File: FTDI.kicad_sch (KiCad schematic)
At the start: 24 parts, among them J301 Conn_01x02_Male, J302 Conn_01x03_Male, SW301 SW_SPDT, U301 SN74LVC257AD, U302 FT232HL, U303 93LC56BT-I/OT, Y301 12MHz

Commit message: Complete Draft 1 of PCB Design
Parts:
- removed J301: Conn_01x02_Male, Connector_PinHeader_2.54mm:PinHeader_1x02_P2.54mm_Vertical, symbol Connector:Conn_01x02_Male
- removed R305: 10K, Resistor_SMD:R_0402_1005Metric, symbol Device:R
- removed SW301: SW_SPDT, Button_Switch_SMD:SW_SPDT_PCM12, symbol Switch:SW_SPDT
- added J301: Conn_01x04_Male, Connector_PinHeader_2.54mm:PinHeader_1x04_P2.54mm_Horizontal, symbol Connector:Conn_01x04_Male
- added J302: Conn_01x03_Male, Connector_PinHeader_2.54mm:PinHeader_1x03_P2.54mm_Horizontal, symbol Connector:Conn_01x03_Male
- renumbered J302 to J303, R306 to R305
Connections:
- net +3V3: now also J302.1 (Pin_1)
- net CONN.SCK: now also J301.2 (Pin_2), J301.4 (Pin_4)
- net CONN.SDA: now also J301.1 (Pin_1), J301.3 (Pin_3)
- net GND: now also J302.3 (Pin_3)
- net MUX.SEL: now also J302.2 (Pin_2)
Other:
- note removed: "Default = FTDI"

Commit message: Draft 1 complete
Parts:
- removed U301: SN74LVC257AD, Package_SO:SOIC-16W_5.3x10.2mm_P1.27mm, symbol 74xx:74LS157
- C301, C302, C303, C304, C305: LCSC (none) -> C1525; LCSC Part Number (none) -> C1525
- C306, C307: LCSC (none) -> C76991; LCSC Part Number (none) -> C76991
- C308, C309: LCSC (none) -> C1557; LCSC Part Number (none) -> C1557
- FB301, FB302: LCSC (none) -> C1002; LCSC Part Number (none) -> C1002
- J301: LCSC (none) -> C91552; LCSC Part Number (none) -> C91552
- J302: footprint Connector_PinHeader_2.54mm:PinHeader_1x03_P2.54mm_Horizontal -> Connector_PinHeader_2.54mm:PinHeader_1x03_P2.54mm_Vertical; LCSC (none) -> C49257; LCSC Part Number (none) -> C49257
- J303: LCSC (none) -> C49257; LCSC Part Number (none) -> C49257
- R301, R302: LCSC (none) -> C140214; LCSC Part Number (none) -> C140214
- R303, R304: LCSC (none) -> C25752; LCSC Part Number (none) -> C25752
- R305: LCSC (none) -> C25879; LCSC Part Number (none) -> C25879
- U301: renamed from U302; value FT232HL -> FT232HQ-REEL; footprint Package_QFP:LQFP-48_7x7mm_P0.5mm -> Package_DFN_QFN:QFN-48-1EP_8x8mm_P0.5mm_EP6.2x6.2mm; LCSC (none) -> C82158; LCSC Part Number (none) -> C82158
- U302: renamed from U303; LCSC (none) -> C190271; LCSC Part Number (none) -> C190271
- Y301: LCSC (none) -> C14871; LCSC Part Number (none) -> C14871
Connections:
- net +3V3: no longer J302.1 (Pin_1), J303.1 (Pin_1)
- net CONN.SCK: now also J303.1 (Pin_1)
- net CONN.SDA: now also J302.1 (Pin_1)
- net FTDI.SCK: now also J303.3 (Pin_3)
- net FTDI.SDA: now also J302.3 (Pin_3)
- net GND: now also U301.49 (GND); no longer J302.3 (Pin_3), J303.3 (Pin_3)
- net IO.SCK: now also J303.2 (Pin_2)
- net IO.SDA: now also J302.2 (Pin_2)
- removed net MUX.SEL: J302.2 (Pin_2), J303.2 (Pin_2)
- no-connect marks 22 -> 16
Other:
- note added: "Jumper Headers for selecting FTDI or Header"
- note added: "Use jumpers to select between modes: Select CONN: CONN.SDA=IO.SDA & CONN.SCK=IO.SCK Select FTDI: FTDI.SDA=IO.SDA & FTDI.SCK=IO.SCK"
- note removed: "MUX for selecting FTDI or Header (Default=FTDI)"
- note removed: "Propagation Delay = 4.6ns"
- note removed: "SEL = L, Output = A = FTDI SEL = H, Output = B = CONN"
- moved on the sheet: J301

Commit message: Complete Design
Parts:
- J302, J303: LCSC C49257 -> (none); LCSC Part Number C49257 -> (none)
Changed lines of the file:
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@@
       (effects (font (size 1.27 1.27)) hide)
     )
-    (property "LCSC" "C49257" (id 4) (at 282.575 36.195 0)
-      (effects (font (size 1.27 1.27)) hide)
-    )
-    (property "LCSC Part Number" "C49257" (id 5) (at 282.575 36.195 0)
+    (property "LCSC" "" (id 4) (at 282.575 36.195 0)
+      (effects (font (size 1.27 1.27)) hide)
+    )
+    (property "LCSC Part Number" "" (id 5) (at 282.575 36.195 0)
       (effects (font (size 1.27 1.27)) hide)
     )
@@
       (effects (font (size 1.27 1.27)) hide)
     )
-    (property "LCSC" "C49257" (id 4) (at 285.115 36.195 0)
-      (effects (font (size 1.27 1.27)) hide)
-    )
-    (property "LCSC Part Number" "C49257" (id 5) (at 285.115 36.195 0)
-      (effects (font (size 1.27 1.27)) hide)
-    )
+    (property "LCSC" "" (id 4) (at 285.115 36.195 0)
+      (effects (font (size 1.27 1.27)) hide)
+    )
+    (property "LCSC Part Number" "" (id 5) (at 285.115 36.195 0)
+      (effects (font (size 1.27 1.27)) hide)
+    )

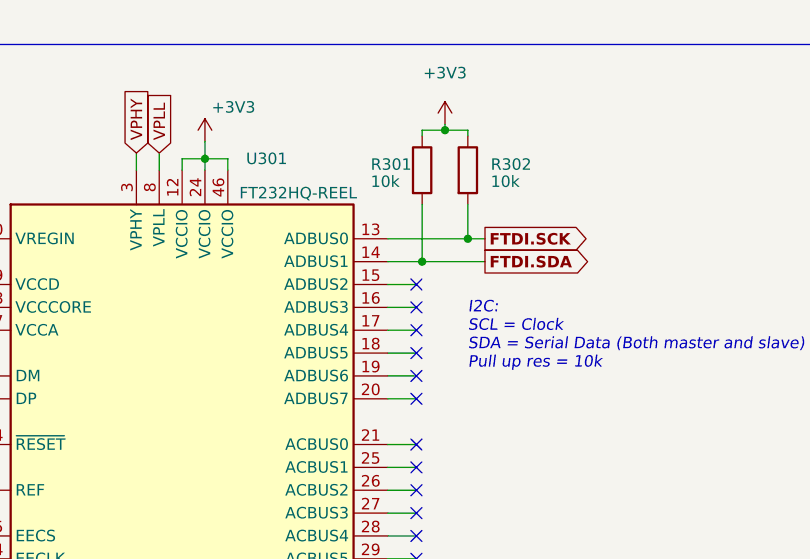
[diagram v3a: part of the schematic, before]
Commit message: Fix FTDI 1 Channel SDA issue
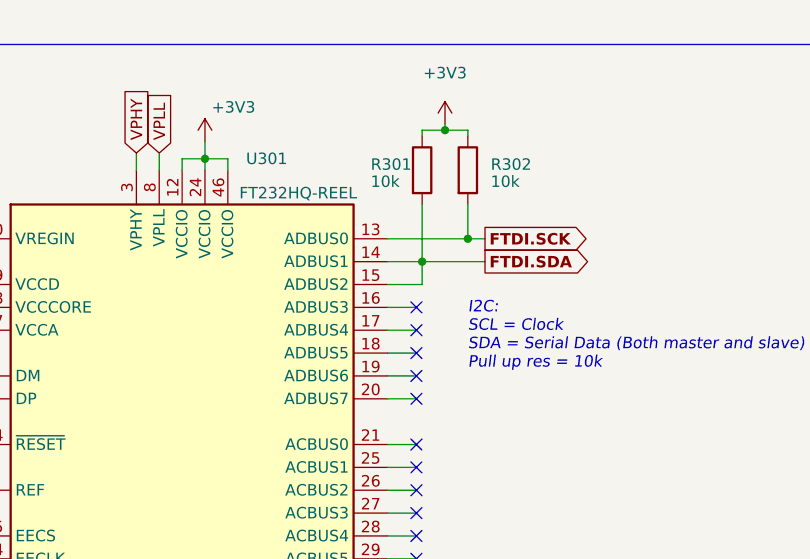
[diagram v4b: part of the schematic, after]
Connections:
- net FTDI.SDA: now also U301.15 (ADBUS2)
- no-connect marks 16 -> 15
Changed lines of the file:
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@@
   (no_connect (at 104.14 63.5))
   (no_connect (at 104.14 53.34))
-  (no_connect (at 104.14 50.8))
   (wire (pts (xy 224.155 68.58) (xy 229.235 68.58))
     (stroke (width 0) (type default) (color 0 0 0 0))
@@
     (stroke (width 0) (type default) (color 0 0 0 0))
   )
+  (wire (pts (xy 104.775 50.8) (xy 104.775 48.26))
+    (stroke (width 0) (type default) (color 0 0 0 0))
+  )
   (wire (pts (xy 104.775 48.26) (xy 111.76 48.26))
     (stroke (width 0) (type default) (color 0 0 0 0))
@@
     (stroke (width 0) (type default) (color 0 0 0 0))
   )
-  (wire (pts (xy 100.965 50.8) (xy 104.14 50.8))
-    (stroke (width 0) (type default) (color 0 0 0 0))
-  )
+  (wire (pts (xy 100.965 50.8) (xy 104.775 50.8))
+    (stroke (width 0) (type default) (color 0 0 0 0))
+  )

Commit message: Complete V1.3
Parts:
- J302, J303: LCSC (none) -> C3012205; LCSC Part Number (none) -> C3012205
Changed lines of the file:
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@@
       (effects (font (size 1.27 1.27)) hide)
     )
-    (property "LCSC" "" (id 4) (at 282.575 36.195 0)
-      (effects (font (size 1.27 1.27)) hide)
-    )
-    (property "LCSC Part Number" "" (id 5) (at 282.575 36.195 0)
+    (property "LCSC" "C3012205" (id 4) (at 282.575 36.195 0)
+      (effects (font (size 1.27 1.27)) hide)
+    )
+    (property "LCSC Part Number" "C3012205" (id 5) (at 282.575 36.195 0)
       (effects (font (size 1.27 1.27)) hide)
     )
@@
       (effects (font (size 1.27 1.27)) hide)
     )
-    (property "LCSC" "" (id 4) (at 285.115 36.195 0)
-      (effects (font (size 1.27 1.27)) hide)
-    )
-    (property "LCSC Part Number" "" (id 5) (at 285.115 36.195 0)
-      (effects (font (size 1.27 1.27)) hide)
-    )
+    (property "LCSC" "C3012205" (id 4) (at 285.115 36.195 0)
+      (effects (font (size 1.27 1.27)) hide)
+    )
+    (property "LCSC Part Number" "C3012205" (id 5) (at 285.115 36.195 0)
+      (effects (font (size 1.27 1.27)) hide)
+    )
